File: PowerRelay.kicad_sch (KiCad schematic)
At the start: 27 parts, among them J1 Screw_Terminal_01x03, J2 Conn_01x20_Female, J3 Conn_01x20_Female, J4 Conn_01x02_Female, J5 Screw_Terminal_01x03, J6 Screw_Terminal_01x03, J7 Conn_01x02_Female, J8 AudioJack4, K1 G5LE-1A4_DC3, K2 G5LE-1A4_DC3, Q1 2N7000, Q2 2N7000

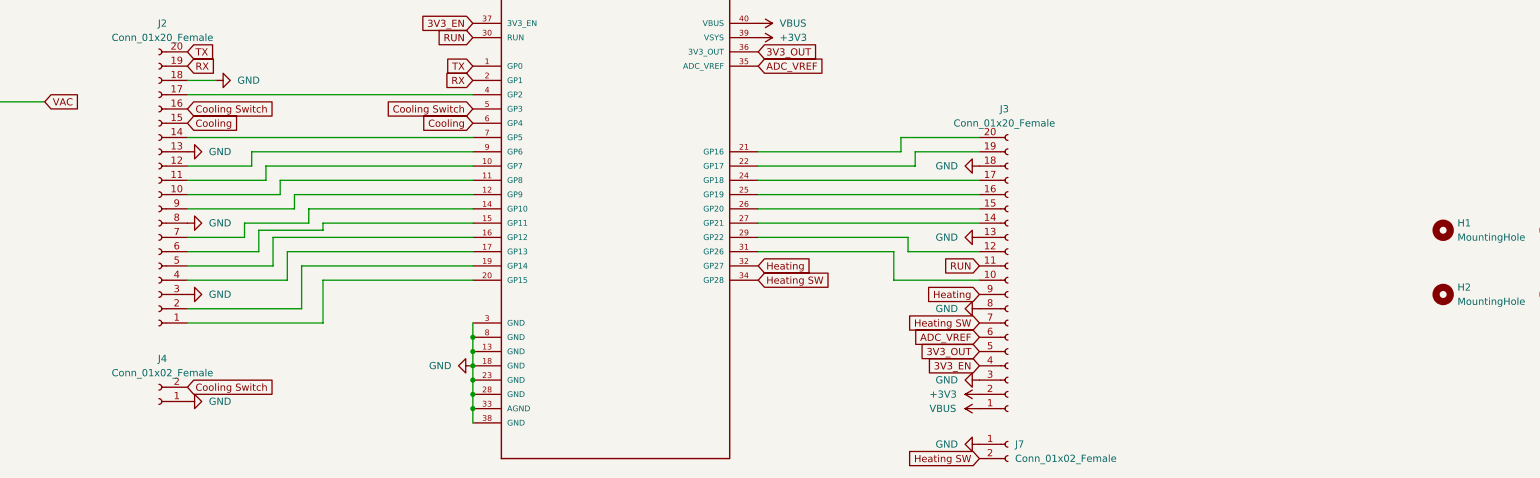
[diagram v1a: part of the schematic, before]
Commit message: add cutout for plugs to sit
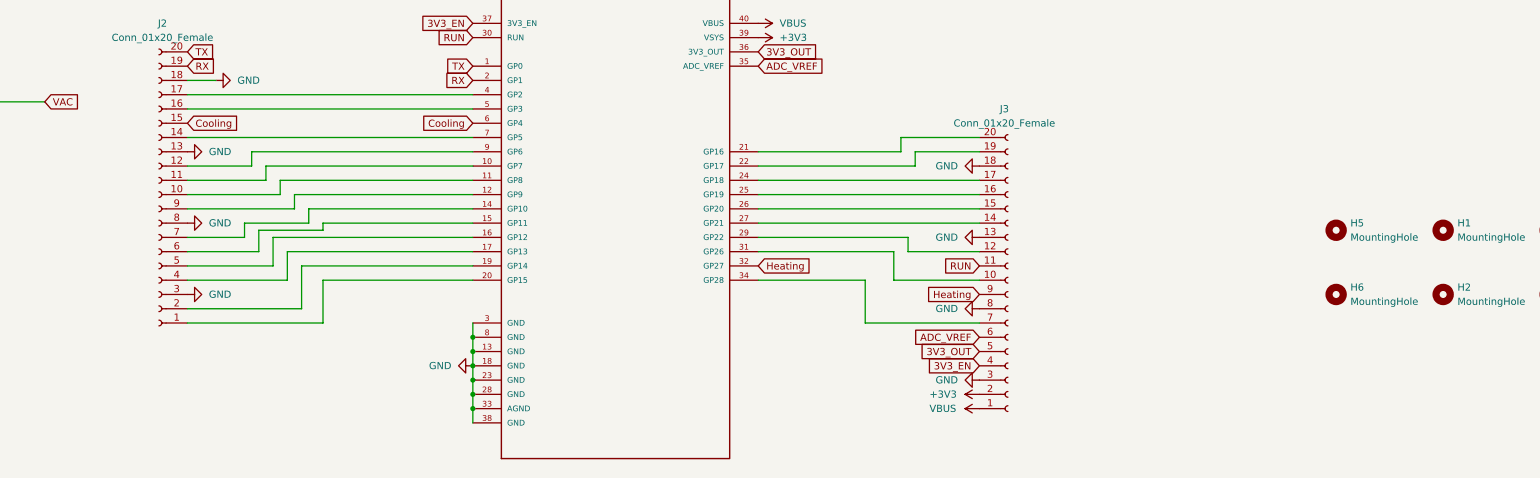
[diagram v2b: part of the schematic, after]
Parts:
- removed J4, J7: Conn_01x02_Female, Connector_PinHeader_2.54mm:PinHeader_1x02_P2.54mm_Vertical, symbol Connector:Conn_01x02_Female
- added H5, H6: MountingHole, MountingHole:MountingHole_3mm, symbol Mechanical:MountingHole
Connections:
- net Cooling Switch: no longer names the net of A1.5 (GP3), J2.16 (Pin_16)
- net Heating SW: no longer names the net of A1.34 (GP28), J3.7 (Pin_7)
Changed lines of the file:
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@@
+    (stroke (width 0) (type default) (color 0 0 0 0))
+  )
+  (wire (pts (xy 213.36 161.29) (xy 233.68 161.29))
     (stroke (width 0) (type default) (color 0 0 0 0))
   )
@@
     (stroke (width 0) (type default) (color 0 0 0 0))
   )
+  (wire (pts (xy 92.71 123.19) (xy 143.51 123.19))
+    (stroke (width 0) (type default) (color 0 0 0 0))
+  )
   (wire (pts (xy 25.4 50.8) (xy 38.1 50.8))
     (stroke (width 0) (type default) (color 0 0 0 0))
@@
     (stroke (width 0) (type default) (color 0 0 0 0))
   )
+  (wire (pts (xy 194.31 153.67) (xy 213.36 153.67))
+    (stroke (width 0) (type default) (color 0 0 0 0))
+  )
   (wire (pts (xy 220.98 146.05) (xy 220.98 148.59))
     (stroke (width 0) (type default) (color 0 0 0 0))
@@
   )
   (wire (pts (xy 106.68 135.89) (xy 92.71 135.89))
+    (stroke (width 0) (type default) (color 0 0 0 0))
+  )
+  (wire (pts (xy 213.36 153.67) (xy 213.36 161.29))
     (stroke (width 0) (type default) (color 0 0 0 0))
   )
@@
     )
   )
-  (global_label "Cooling Switch" (shape input) (at 92.71 123.19 0) (fields_autoplaced)
-    (effects (font (size 1.27 1.27)) (justify left))
-    (property "Intersheet References" "${INTERSHEET_REFS}" (id 0) (at 109.335 123.1106 0)
-      (effects (font (size 1.27 1.27)) (justify left) hide)
-    )
-  )
   (global_label "ADC_VREF" (shape input) (at 194.31 115.57 0) (fields_autoplaced)
     (effects (font (size 1.27 1.27)) (justify left))
     (property "Intersheet References" "${INTERSHEET_REFS}" (id 0) (at 205.9155 115.4906 0)
       (effects (font (size 1.27 1.27)) (justify left) hide)
-    )
-  )
-  (global_label "Heating SW" (shape input) (at 233.68 185.42 180) (fields_autoplaced)
-    (effects (font (size 1.27 1.27)) (justify right))
-    (property "Intersheet References" "${INTERSHEET_REFS}" (id 0) (at 220.4417 185.4994 0)
-      (effects (font (size 1.27 1.27)) (justify right) hide)
     )
   )
@@
     )
   )
-  (global_label "Cooling Switch" (shape input) (at 143.51 123.19 180) (fields_autoplaced)
-    (effects (font (size 1.27 1.27)) (justify right))
-    (property "Intersheet References" "${INTERSHEET_REFS}" (id 0) (at 126.885 123.2694 0)
-      (effects (font (size 1.27 1.27)) (justify right) hide)
-    )
-  )
   (global_label "ADC_VREF" (shape input) (at 233.68 163.83 180) (fields_autoplaced)
     (effects (font (size 1.27 1.27)) (justify right))
@@
     )
   )
-  (global_label "Heating SW" (shape input) (at 194.31 153.67 0) (fields_autoplaced)
-    (effects (font (size 1.27 1.27)) (justify left))
-    (property "Intersheet References" "${INTERSHEET_REFS}" (id 0) (at 207.5483 153.5906 0)
-      (effects (font (size 1.27 1.27)) (justify left) hide)
-    )
-  )
   (global_label "VAC" (shape input) (at 312.42 85.09 180) (fields_autoplaced)
     (effects (font (size 1.27 1.27)) (justify right))
@@
     )
   )
-  (global_label "Cooling Switch" (shape input) (at 92.71 172.72 0) (fields_autoplaced)
-    (effects (font (size 1.27 1.27)) (justify left))
-    (property "Intersheet References" "${INTERSHEET_REFS}" (id 0) (at 109.335 172.6406 0)
-      (effects (font (size 1.27 1.27)) (justify left) hide)
-    )
-  )
-  (global_label "Heating SW" (shape input) (at 233.68 161.29 180) (fields_autoplaced)
-    (effects (font (size 1.27 1.27)) (justify right))
-    (property "Intersheet References" "${INTERSHEET_REFS}" (id 0) (at 220.4417 161.3694 0)
-      (effects (font (size 1.27 1.27)) (justify right) hide)
-    )
-  )
   (global_label "VAC" (shape input) (at 312.42 55.88 180) (fields_autoplaced)
     (effects (font (size 1.27 1.27)) (justify right))
@@
     (pin "TX")
   )
+  (symbol (lib_id "Mechanical:MountingHole") (at 297.18 156.21 0) (unit 1)
+    (in_bom yes) (on_board yes) (fields_autoplaced)
+    (property "Reference" "H6" (id 0) (at 299.72 154.9399 0)
+      (effects (font (size 1.27 1.27)) (justify left))
+    )
+    (property "Value" "MountingHole" (id 1) (at 299.72 157.4799 0)
+      (effects (font (size 1.27 1.27)) (justify left))
+    )
+    (property "Footprint" "MountingHole:MountingHole_3mm" (id 2) (at 297.18 156.21 0)
+      (effects (font (size 1.27 1.27)) hide)
+    )
+    (property "Datasheet" "~" (id 3) (at 297.18 156.21 0)
+      (effects (font (size 1.27 1.27)) hide)
+    )
+  )
   (symbol (lib_id "power:GND") (at 308.61 66.04 0) (unit 1)
     (in_bom yes) (on_board yes) (fields_autoplaced)
@@
     )
     (property "Datasheet" "" (id 3) (at 133.35 50.8 0)
-      (effects (font (size 1.27 1.27)) hide)
-    )
-    (pin "1")
-  )
-  (symbol (lib_id "power:GND") (at 92.71 175.26 90) (unit 1)
-    (in_bom yes) (on_board yes) (fields_autoplaced)
-    (property "Reference" "#PWR0130" (id 0) (at 99.06 175.26 0)
-      (effects (font (size 1.27 1.27)) hide)
-    )
-    (property "Value" "GND" (id 1) (at 96.52 175.2599 90)
-      (effects (font (size 1.27 1.27)) (justify right))
-    )
-    (property "Footprint" "" (id 2) (at 92.71 175.26 0)
-      (effects (font (size 1.27 1.27)) hide)
-    )
-    (property "Datasheet" "" (id 3) (at 92.71 175.26 0)
       (effects (font (size 1.27 1.27)) hide)
     )
@@
     (pin "1")
   )
-  (symbol (lib_id "Connector:Conn_01x02_Female") (at 238.76 182.88 0) (unit 1)
-    (in_bom yes) (on_board yes) (fields_autoplaced)
-    (property "Reference" "J7" (id 0) (at 240.03 182.8799 0)
-      (effects (font (size 1.27 1.27)) (justify left))
-    )
-    (property "Value" "Conn_01x02_Female" (id 1) (at 240.03 185.4199 0)
-      (effects (font (size 1.27 1.27)) (justify left))
-    )
-    (property "Footprint" "Connector_PinHeader_2.54mm:PinHeader_1x02_P2.54mm_Vertical" (id 2) (at 238.76 182.88 0)
-      (effects (font (size 1.27 1.27)) hide)
-    )
-    (property "Datasheet" "~" (id 3) (at 238.76 182.88 0)
-      (effects (font (size 1.27 1.27)) hide)
-    )
-    (pin "1")
-    (pin "2")
-  )
   (symbol (lib_id "power:Earth") (at 377.19 87.63 270) (unit 1)
     (in_bom yes) (on_board yes) (fields_autoplaced)
@@
     )
   )
-  (symbol (lib_id "power:GND") (at 233.68 182.88 270) (unit 1)
-    (in_bom yes) (on_board yes) (fields_autoplaced)
-    (property "Reference" "#PWR0129" (id 0) (at 227.33 182.88 0)
-      (effects (font (size 1.27 1.27)) hide)
-    )
-    (property "Value" "GND" (id 1) (at 229.87 182.8799 90)
-      (effects (font (size 1.27 1.27)) (justify right))
-    )
-    (property "Footprint" "" (id 2) (at 233.68 182.88 0)
-      (effects (font (size 1.27 1.27)) hide)
-    )
-    (property "Datasheet" "" (id 3) (at 233.68 182.88 0)
-      (effects (font (size 1.27 1.27)) hide)
-    )
-    (pin "1")
-  )
   (symbol (lib_id "Device:D_Schottky") (at 308.61 91.44 270) (unit 1)
     (in_bom yes) (on_board yes) (fields_autoplaced)
@@
     )
     (pin "1")
+  )
+  (symbol (lib_id "Mechanical:MountingHole") (at 297.18 144.78 0) (unit 1)
+    (in_bom yes) (on_board yes) (fields_autoplaced)
+    (property "Reference" "H5" (id 0) (at 299.72 143.5099 0)
+      (effects (font (size 1.27 1.27)) (justify left))
+    )
+    (property "Value" "MountingHole" (id 1) (at 299.72 146.0499 0)
+      (effects (font (size 1.27 1.27)) (justify left))
+    )
+    (property "Footprint" "MountingHole:MountingHole_3mm" (id 2) (at 297.18 144.78 0)
+      (effects (font (size 1.27 1.27)) hide)
+    )
+    (property "Datasheet" "~" (id 3) (at 297.18 144.78 0)
+      (effects (font (size 1.27 1.27)) hide)
+    )
   )
   (symbol (lib_id "Connector:Screw_Terminal_01x03") (at 26.67 121.92 180) (unit 1)
@@
     (pin "1")
   )
-  (symbol (lib_id "Connector:Conn_01x02_Female") (at 87.63 175.26 180) (unit 1)
-    (in_bom yes) (on_board yes) (fields_autoplaced)
-    (property "Reference" "J4" (id 0) (at 88.265 167.64 0))
-    (property "Value" "Conn_01x02_Female" (id 1) (at 88.265 170.18 0))
-    (property "Footprint" "Connector_PinHeader_2.54mm:PinHeader_1x02_P2.54mm_Vertical" (id 2) (at 87.63 175.26 0)
-      (effects (font (size 1.27 1.27)) hide)
-    )
-    (property "Datasheet" "~" (id 3) (at 87.63 175.26 0)
-      (effects (font (size 1.27 1.27)) hide)
-    )
-    (pin "1")
-    (pin "2")
-  )
   (symbol (lib_id "power:GND") (at 92.71 143.51 90) (unit 1)
     (in_bom yes) (on_board yes) (fields_autoplaced)
@@
       (reference "#PWR0128") (unit 1) (value "Earth") (footprint "")
     )
-    (path "/acb13578-5109-4b50-914c-c9abc815a49b"
-      (reference "#PWR0129") (unit 1) (value "GND") (footprint "")
-    )
-    (path "/48460d7d-bd71-47f2-aa0c-14f4943a8430"
-      (reference "#PWR0130") (unit 1) (value "GND") (footprint "")
-    )
     (path "/058564c8-d209-4734-add6-195b3e479042"
       (reference "#PWR0131") (unit 1) (value "+3V3") (footprint "")
@@
       (reference "H4") (unit 1) (value "MountingHole") (footprint "MountingHole:MountingHole_3mm")
     )
+    (path "/c081b96e-0b0f-4ef0-bf28-677d9edbaf46"
+      (reference "H5") (unit 1) (value "MountingHole") (footprint "MountingHole:MountingHole_3mm")
+    )
+    (path "/131f8ef3-4ce9-4a79-b966-2078febcf498"
+      (reference "H6") (unit 1) (value "MountingHole") (footprint "MountingHole:MountingHole_3mm")
+    )
     (path "/c51f0dd0-a639-41a4-86ca-307a729d7147"
       (reference "J1") (unit 1) (value "Screw_Terminal_01x03") (footprint "KiCad2:1760520000")
@@
       (reference "J3") (unit 1) (value "Conn_01x20_Female") (footprint "Connector_PinHeader_2.54mm:PinHeader_1x20_P2.54mm_Vertical")
     )
-    (path "/e2019170-a35d-4646-878c-a7e30159e571"
-      (reference "J4") (unit 1) (value "Conn_01x02_Female") (footprint "Connector_PinHeader_2.54mm:PinHeader_1x02_P2.54mm_Vertical")
-    )
     (path "/9269b1e9-9a48-4f78-b9ae-1f98ff93bbda"
       (reference "J5") (unit 1) (value "Screw_Terminal_01x03") (footprint "KiCad2:1760520000")
@@
       (reference "J6") (unit 1) (value "Screw_Terminal_01x03") (footprint "KiCad2:1760520000")
     )
-    (path "/8414043a-5d70-4833-8d66-3113c9aa58d9"
-      (reference "J7") (unit 1) (value "Conn_01x02_Female") (footprint "Connector_PinHeader_2.54mm:PinHeader_1x02_P2.54mm_Vertical")
-    )
     (path "/0faf3218-cf03-4891-a339-737e2b007313"
